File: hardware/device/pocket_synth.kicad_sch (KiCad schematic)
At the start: 7 parts

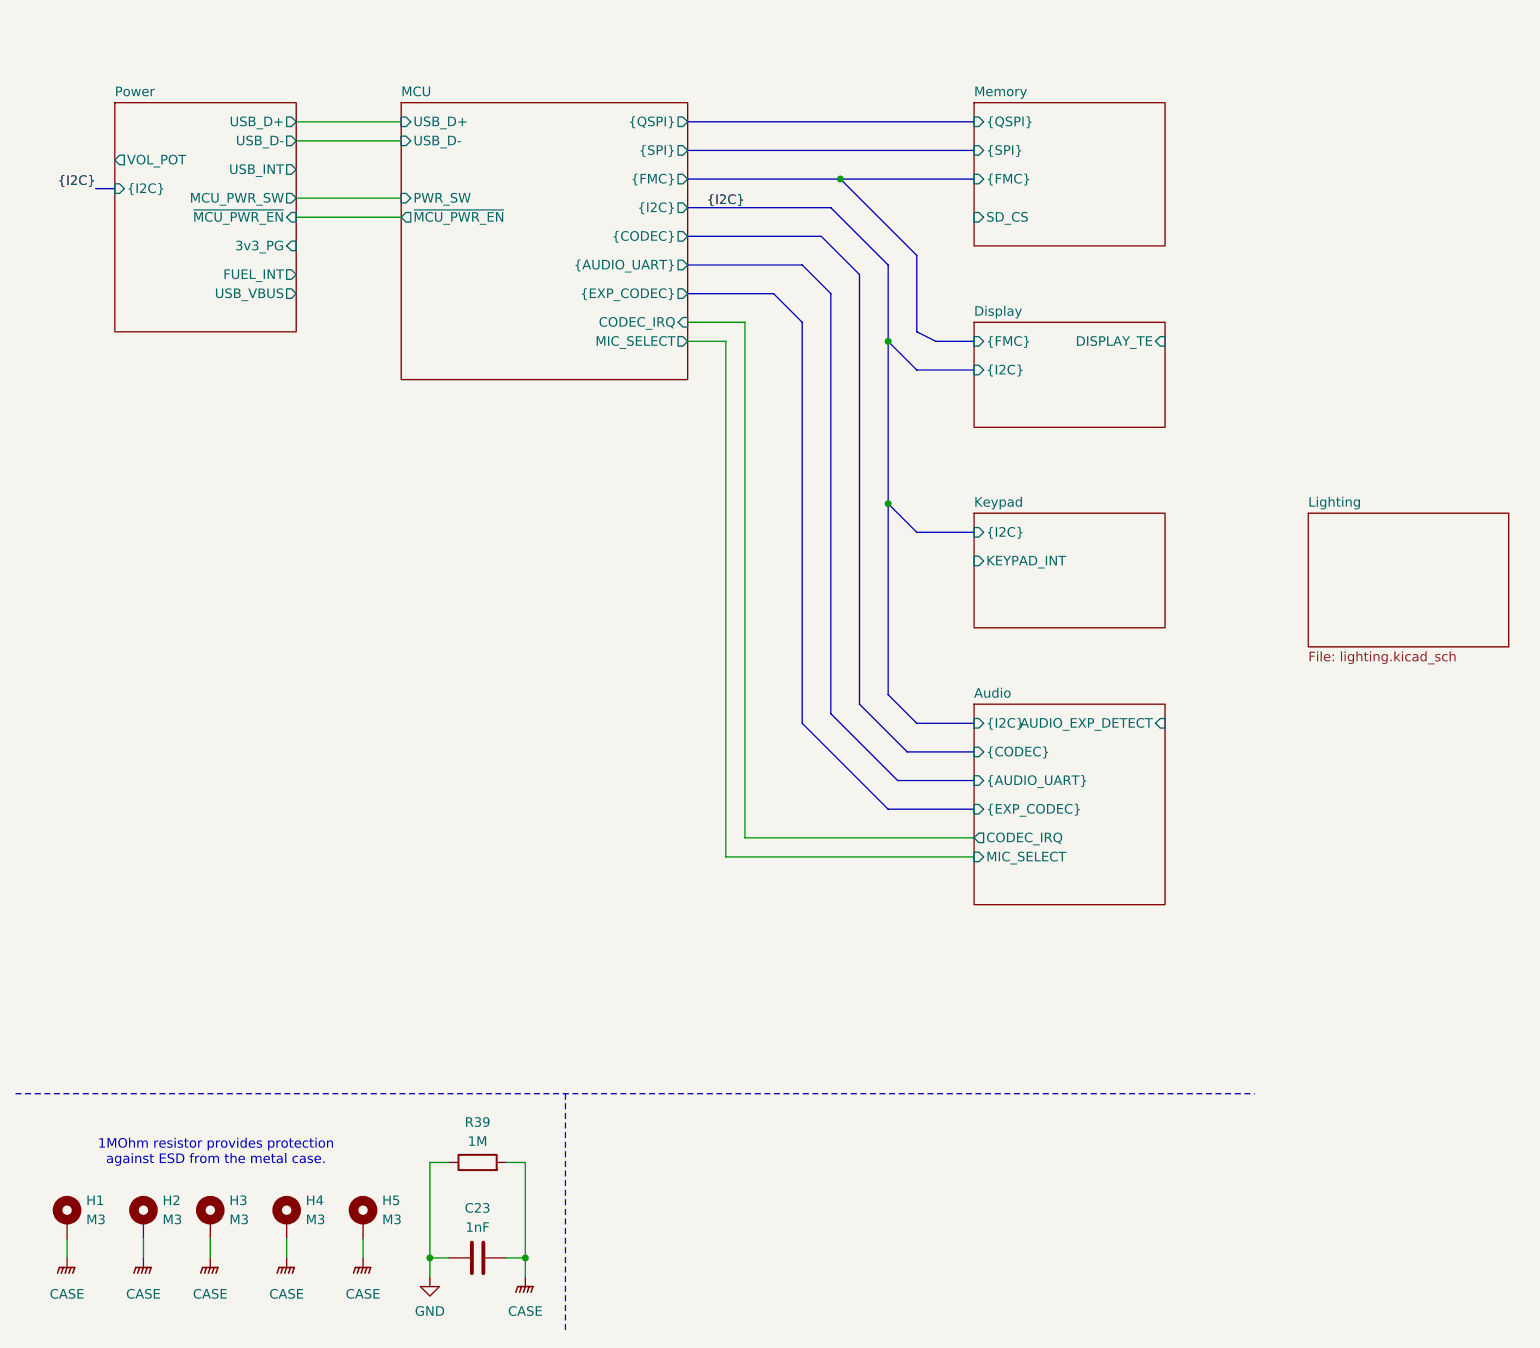
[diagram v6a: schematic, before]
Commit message: feat: various routing, footprint and schematic cleanup
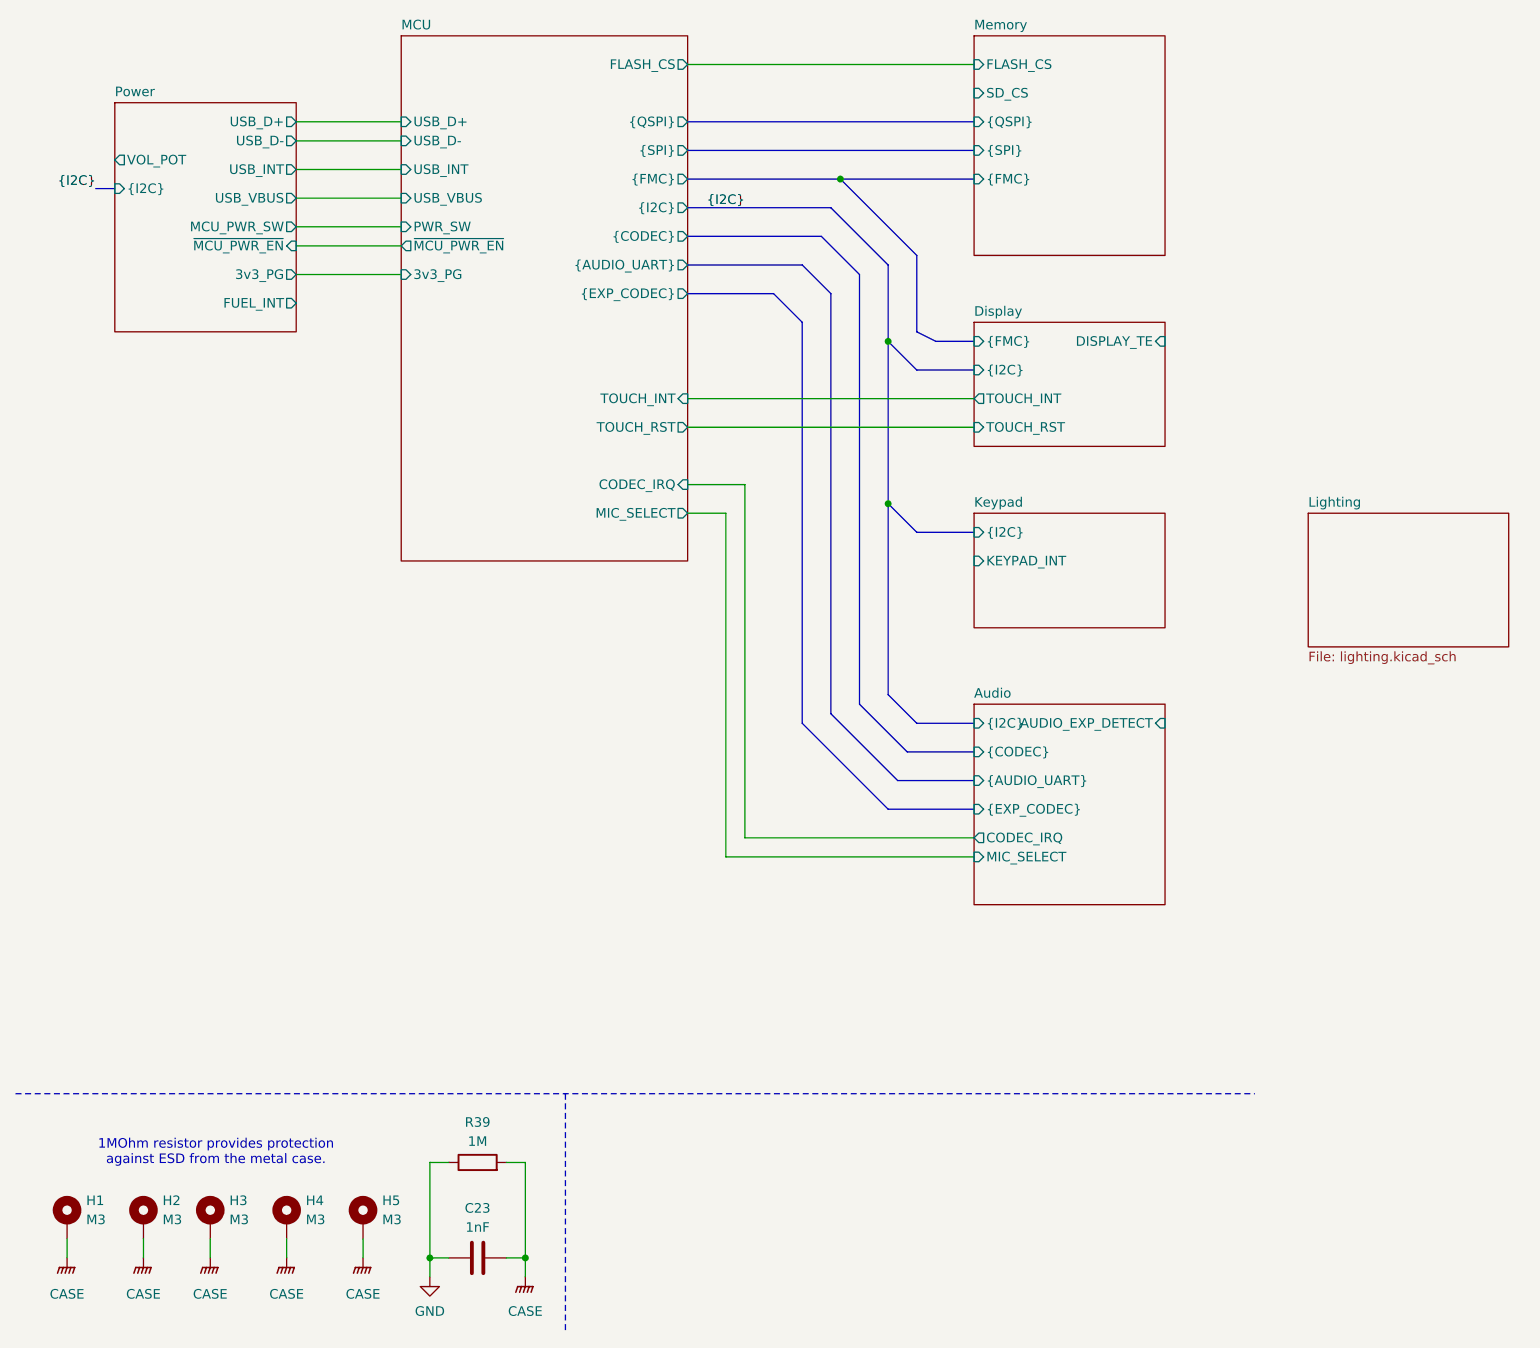
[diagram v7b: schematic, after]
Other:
- sheet Display ports: added TOUCH_INT, TOUCH_RST; removed none
- sheet MCU ports: added 3v3_PG, FLASH_CS, TOUCH_INT, TOUCH_RST, USB_INT, USB_VBUS; removed none
- sheet Memory ports: added FLASH_CS; removed none
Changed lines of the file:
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@@
+	(wire
+		(pts
+			(xy 49.53 46.99) (xy 63.5 46.99)
+		)
+		(stroke
+			(width 0)
+			(type default)
+		)
+	)
 	(wire
 		(pts
@@
 		)
 	)
+	(wire
+		(pts
+			(xy 101.6 73.66) (xy 139.7 73.66)
+		)
+		(stroke
+			(width 0)
+			(type default)
+		)
+	)
 	(bus
 		(pts
@@
 		)
 	)
+	(wire
+		(pts
+			(xy 49.53 57.15) (xy 63.5 57.15)
+		)
+		(stroke
+			(width 0)
+			(type default)
+		)
+	)
 	(bus
 		(pts
@@
 	(wire
 		(pts
-			(xy 109.22 63.5) (xy 109.22 132.08)
+			(xy 109.22 85.09) (xy 109.22 132.08)
 		)
 		(stroke
@@
 	(wire
 		(pts
-			(xy 101.6 66.04) (xy 106.68 66.04)
+			(xy 101.6 88.9) (xy 106.68 88.9)
 		)
 		(stroke
@@
 	(wire
 		(pts
-			(xy 101.6 63.5) (xy 109.22 63.5)
+			(xy 101.6 85.09) (xy 109.22 85.09)
 		)
 		(stroke
@@
 		)
 	)
+	(wire
+		(pts
+			(xy 101.6 77.47) (xy 139.7 77.47)
+		)
+		(stroke
+			(width 0)
+			(type default)
+		)
+	)
 	(bus
 		(pts
@@
 	(wire
 		(pts
-			(xy 106.68 66.04) (xy 106.68 134.62)
+			(xy 106.68 88.9) (xy 106.68 134.62)
 		)
 		(stroke
@@
 		)
 	)
+	(wire
+		(pts
+			(xy 101.6 29.21) (xy 139.7 29.21)
+		)
+		(stroke
+			(width 0)
+			(type default)
+		)
+	)
 	(polyline
 		(pts
@@
 		)
 	)
+	(wire
+		(pts
+			(xy 49.53 43.18) (xy 63.5 43.18)
+		)
+		(stroke
+			(width 0)
+			(type default)
+		)
+	)
 	(bus
 		(pts
@@
 	(wire
 		(pts
-			(xy 49.53 49.53) (xy 63.5 49.53)
+			(xy 49.53 53.34) (xy 63.5 53.34)
 		)
 		(stroke
@@
 	(wire
 		(pts
-			(xy 49.53 46.99) (xy 63.5 46.99)
+			(xy 49.53 50.8) (xy 63.5 50.8)
 		)
 		(stroke
@@
 	)
 	(sheet
-		(at 63.5 34.29)
-		(size 38.1 36.83)
+		(at 63.5 25.4)
+		(size 38.1 69.85)
 		(exclude_from_sim no)
 		(in_bom yes)
@@
 		)
 		(property "Sheetname" "MCU"
-			(at 63.5 33.5784 0)
+			(at 63.5 24.6884 0)
 			(effects
 				(font
@@
 		)
 		(property "Sheetfile" "MCU.kicad_sch"
-			(at 63.5 71.7046 0)
+			(at 63.5 95.8346 0)
 			(effects
 				(font
@@
 		)
 		(pin "PWR_SW" input
-			(at 63.5 46.99 180)
+			(at 63.5 50.8 180)
 			(effects
 				(font
@@
 		)
 		(pin "~{MCU_PWR_EN}" output
-			(at 63.5 49.53 180)
+			(at 63.5 53.34 180)
 			(effects
 				(font
@@
 		)
 		(pin "CODEC_IRQ" input
-			(at 101.6 63.5 0)
+			(at 101.6 85.09 0)
 			(effects
 				(font
@@
 		)
 		(pin "MIC_SELECT" output
-			(at 101.6 66.04 0)
+			(at 101.6 88.9 0)
 			(effects
 				(font
@@
 				)
 				(justify right)
+			)
+		)
+		(pin "TOUCH_INT" input
+			(at 101.6 73.66 0)
+			(effects
+				(font
+					(size 1.27 1.27)
+				)
+				(justify right)
+			)
+		)
+		(pin "TOUCH_RST" output
+			(at 101.6 77.47 0)
+			(effects
+				(font
+					(size 1.27 1.27)
+				)
+				(justify right)
+			)
+		)
+		(pin "FLASH_CS" output
+			(at 101.6 29.21 0)
+			(effects
+				(font
+					(size 1.27 1.27)
+				)
+				(justify right)
+			)
+		)
+		(pin "USB_INT" input
+			(at 63.5 43.18 180)
+			(effects
+				(font
+					(size 1.27 1.27)
+				)
+				(justify left)
+			)
+		)
+		(pin "USB_VBUS" input
+			(at 63.5 46.99 180)
+			(effects
+				(font
+					(size 1.27 1.27)
+				)
+				(justify left)
+			)
+		)
+		(pin "3v3_PG" input
+			(at 63.5 57.15 180)
+			(effects
+				(font
+					(size 1.27 1.27)
+				)
+				(justify left)
 			)
 		)
@@
 			)
 		)
-		(pin "3v3_PG" input
-			(at 49.53 53.34 0)
+		(pin "3v3_PG" output
+			(at 49.53 57.15 0)
 			(effects
 				(font
@@
 		)
 		(pin "MCU_PWR_SW" output
-			(at 49.53 46.99 0)
+			(at 49.53 50.8 0)
 			(effects
 				(font
@@
 		)
 		(pin "~{MCU_PWR_EN}" input
-			(at 49.53 49.53 0)
+			(at 49.53 53.34 0)
 			(effects
 				(font
@@
 		)
 		(pin "FUEL_INT" output
-			(at 49.53 57.15 0)
+			(at 49.53 60.96 0)
 			(effects
 				(font
@@
 		)
 		(pin "USB_VBUS" output
-			(at 49.53 59.69 0)
+			(at 49.53 46.99 0)
 			(effects
 				(font
@@
 	)
 	(sheet
-		(at 139.7 34.29)
-		(size 25.4 19.05)
+		(at 139.7 25.4)
+		(size 25.4 29.21)
 		(exclude_from_sim no)
 		(in_bom yes)
@@
 		)
 		(property "Sheetname" "Memory"
-			(at 139.7 33.5784 0)
+			(at 139.7 24.6884 0)
 			(effects
 				(font
@@
 		)
 		(property "Sheetfile" "memory.kicad_sch"
-			(at 139.7 53.9246 0)
+			(at 139.7 55.1946 0)
 			(effects
 				(font
@@
 		)
 		(pin "SD_CS" input
-			(at 139.7 49.53 180)
+			(at 139.7 33.02 180)
 			(effects
 				(font
@@
 		(pin "{QSPI}" input
 			(at 139.7 36.83 180)
+			(effects
+				(font
+					(size 1.27 1.27)
+				)
+				(justify left)
+			)
+		)
+		(pin "FLASH_CS" input
+			(at 139.7 29.21 180)
 			(effects
 				(font
@@
 	(sheet
 		(at 139.7 63.5)
-		(size 25.4 13.97)
+		(size 25.4 16.51)
 		(exclude_from_sim no)
 		(in_bom yes)
@@
 		)
 		(property "Sheetfile" "display.kicad_sch"
-			(at 139.7 78.0546 0)
+			(at 139.7 80.5946 0)
 			(effects
 				(font
@@
 			)
 		)
+		(pin "TOUCH_INT" output
+			(at 139.7 73.66 180)
+			(effects
+				(font
+					(size 1.27 1.27)
+				)
+				(justify left)
+			)
+		)
+		(pin "TOUCH_RST" input
+			(at 139.7 77.47 180)
+			(effects
+				(font
+					(size 1.27 1.27)
+				)
+				(justify left)
+			)
+		)
